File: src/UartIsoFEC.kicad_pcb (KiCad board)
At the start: 2 copper layers, 24 x 27.9 mm, 33 parts, among them J1 B3B-XH-A, P1 105444-0001, Q1 DMP3099L-13, U1 FT230XS, U2 ADUM5211

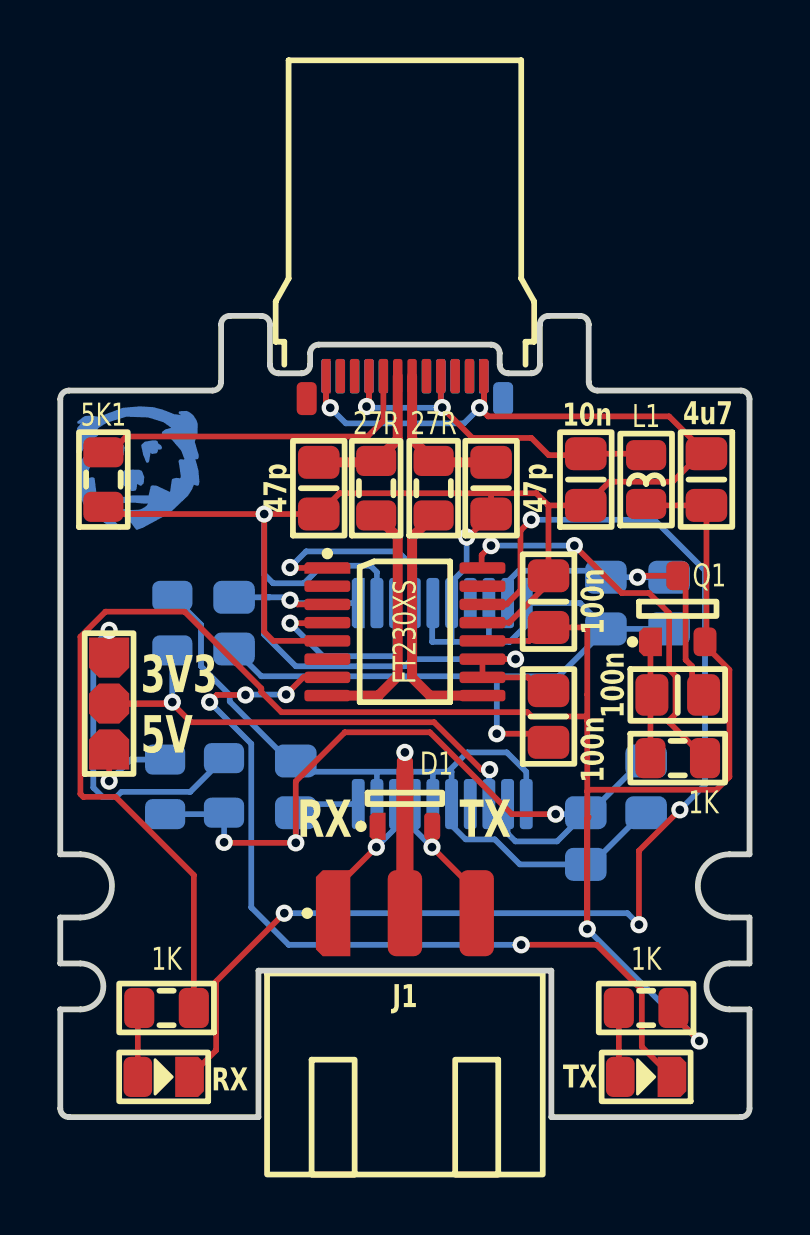
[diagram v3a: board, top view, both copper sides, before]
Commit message: Added RTS/CTS loopback
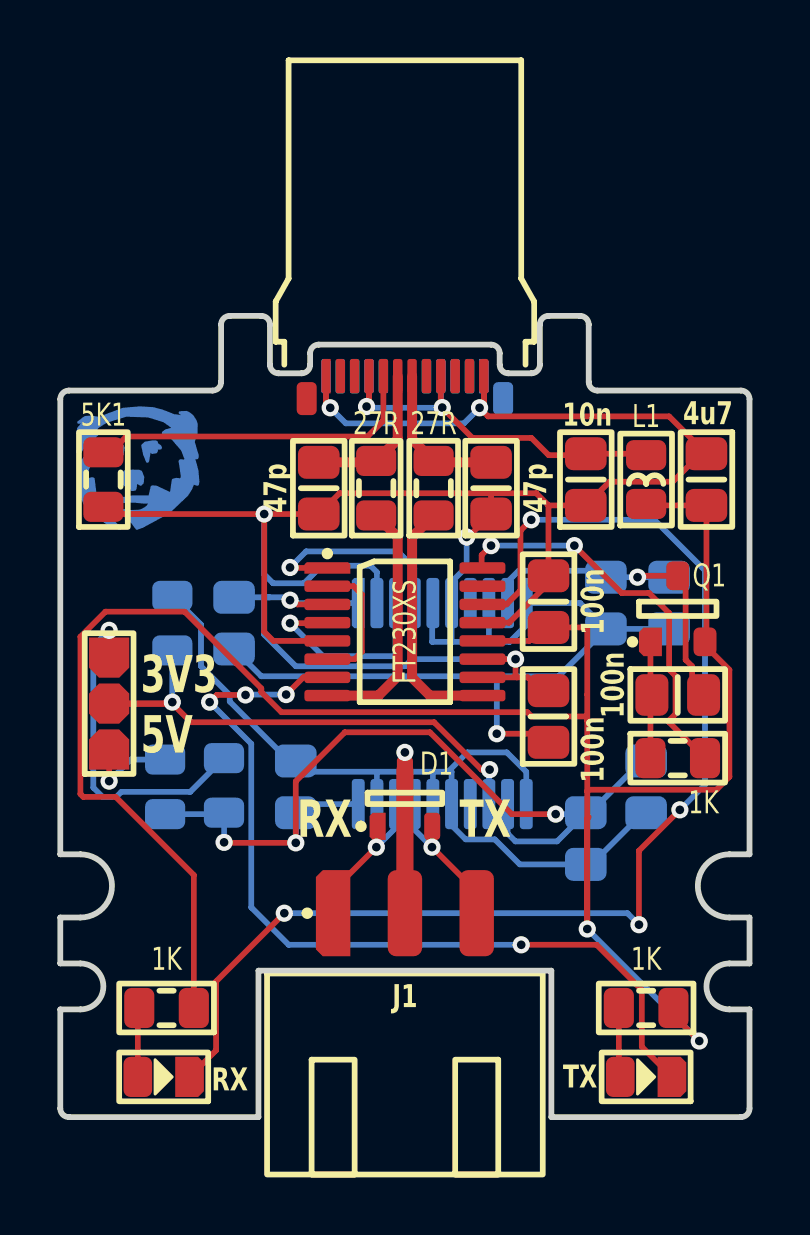
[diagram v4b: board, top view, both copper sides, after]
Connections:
- U1 pad 2: (no net) -> CTS_RTS
- U1 pad 6: (no net) -> CTS_RTS
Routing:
- net CTS_RTS: track 0.00 -> 4.62 mm
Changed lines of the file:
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@@
   (net 24 "ISO_V_SELECT_5V")
   (net 25 "ISO_V_SELECT_3V3")
+  (net 26 "CTS_RTS")
   (footprint "Medo64:R (0805)" (layer "F.Cu")
     (at 40.4 44.1 180)
@@
       (net 22 "TX") (thermal_bridge_angle 45))
     (pad "2" smd roundrect locked (at -2.7 -1.5875) (size 1.6 0.4) (layers "F.Cu" "F.Paste" "F.Mask") (roundrect_rratio 0.25)
-      (thermal_bridge_angle 45))
+      (net 26 "CTS_RTS") (thermal_bridge_angle 45))
     (pad "3" smd roundrect locked (at -2.7 -0.9525) (size 1.6 0.4) (layers "F.Cu" "F.Paste" "F.Mask") (roundrect_rratio 0.25)
       (net 12 "3V3") (thermal_bridge_angle 45))
@@
       (net 1 "GND") (thermal_bridge_angle 45))
     (pad "6" smd roundrect locked (at -2.7 0.9525) (size 1.6 0.4) (layers "F.Cu" "F.Paste" "F.Mask") (roundrect_rratio 0.25)
-      (thermal_bridge_angle 45))
+      (net 26 "CTS_RTS") (thermal_bridge_angle 45))
     (pad "7" smd roundrect locked (at -2.7 1.5875) (size 1.6 0.4) (layers "F.Cu" "F.Paste" "F.Mask") (roundrect_rratio 0.25)
       (net 17 "LED_TX") (thermal_bridge_angle 45))
@@
   (segment (start 37.899998 28) (end 37.899999 27.999999) (width 0.2) (layer "B.Cu") (net 11))
   (segment (start 28.2475 30.0475) (end 29.3 30.0475) (width 0.2) (layer "F.Cu") (net 12))
+  (segment (start 35.8525 32.54) (end 35.9 32.5875) (width 0.2) (layer "F.Cu") (net 12))
   (segment (start 34.7 31.9525) (end 35.8525 31.9525) (width 0.2) (layer "F.Cu") (net 12))
   (segment (start 28 29.8) (end 28.2475 30.0475) (width 0.2) (layer "F.Cu") (net 12))
+  (segment (start 35.9 32.5875) (end 36.2875 32.5875) (width 0.2) (layer "F.Cu") (net 12))
   (segment (start 36.2875 32.5875) (end 36.95 33.25) (width 0.2) (layer "F.Cu") (net 12))
-  (segment (start 34.7 32.5875) (end 36.2875 32.5875) (width 0.2) (layer "F.Cu") (net 12))
-  (segment (start 34.7 32.5875) (end 34.7 31.9525) (width 0.2) (layer "F.Cu") (net 12))
+  (segment (start 34.7 32.5875) (end 35.9 32.5875) (width 0.2) (layer "F.Cu") (net 12))
+  (segment (start 35.8525 31.9525) (end 35.8525 32.54) (width 0.2) (layer "F.Cu") (net 12))
   (via (at 35.8525 31.9525) (size 0.6) (drill 0.3) (layers "F.Cu" "B.Cu") (net 12))
   (via (at 28 29.9) (size 0.6) (drill 0.3) (layers "F.Cu" "B.Cu") (net 12))
@@
   (segment (start 24.525 36.575) (end 22.125 36.575) (width 0.2) (layer "B.Cu") (net 25))
   (segment (start 25.7 35.4) (end 24.525 36.575) (width 0.2) (layer "B.Cu") (net 25))
+  (segment (start 30.2125 29.4125) (end 29.3 29.4125) (width 0.2) (layer "F.Cu") (net 26))
+  (segment (start 30.5 31.7) (end 30.5 29.7) (width 0.2) (layer "F.Cu") (net 26))
+  (segment (start 30.2475 31.9525) (end 30.5 31.7) (width 0.2) (layer "F.Cu") (net 26))
+  (segment (start 30.5 29.7) (end 30.2125 29.4125) (width 0.2) (layer "F.Cu") (net 26))
+  (segment (start 29.3 31.9525) (end 30.2475 31.9525) (width 0.2) (layer "F.Cu") (net 26))
 )

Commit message: Moved LEDs to bottom
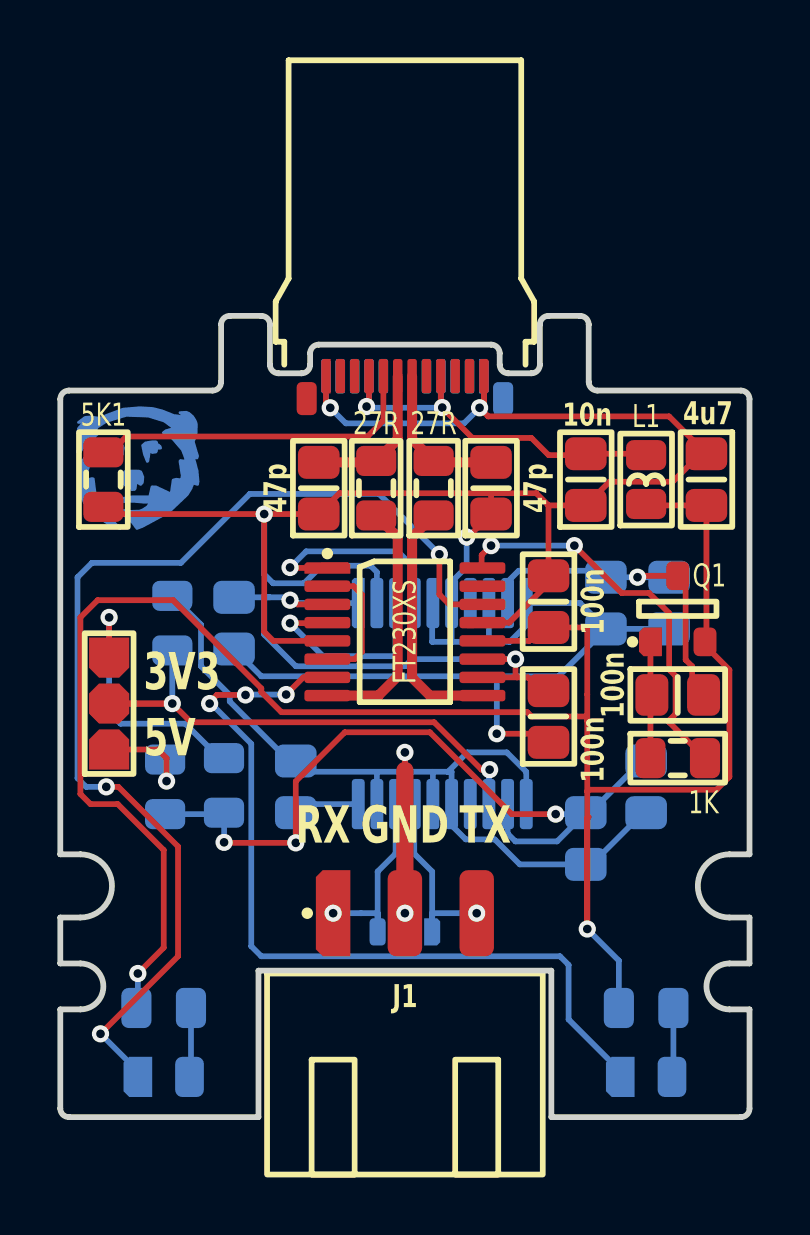
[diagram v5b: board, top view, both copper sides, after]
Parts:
- D1, DS1, DS2, R3, R4: moved to B.Cu
- moved D1 3.68 mm to (32.0, 40.5), turned to 180 degrees
- moved R3 0.10 mm to (23.6, 44.1), turned to 0 degrees
- turned DS1 to 0 degrees
- turned DS2 to 0 degrees
- turned R4 to 0 degrees
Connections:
- D1 pad 1: ISO_RX -> ISO_TX
- D1 pad 2: ISO_TX -> ISO_RX
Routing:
- net LED_RX: track 43.8 -> 38.7 mm, vias 4 -> 3
- net 5V: track 76.7 -> 73.6 mm
- net ISO_V_SELECT_3V3: track 11.9 -> 9.21 mm
- net ISO_TX: track 3.95 -> 6.17 mm
- net ISO_RX: track 3.91 -> 6.10 mm
- net ISO_GND: track 34.3 -> 35.7 mm, vias 1 -> 2
- net LED_TX: track 30.5 -> 29.3 mm, vias 4 -> 3
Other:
- board text added: "GND"

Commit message: Refactored LED control
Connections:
- R3 pad 1: 5V -> 5V_SWITCHED
- R4 pad 1: 5V -> 5V_SWITCHED
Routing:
- net 5V: track 73.6 -> 14.9 mm, vias 2 -> 0
- net 5V_SWITCHED: track 10.5 -> 49.6 mm, vias 1 -> 5
- net PWREN#: track 13.8 -> 15.1 mm

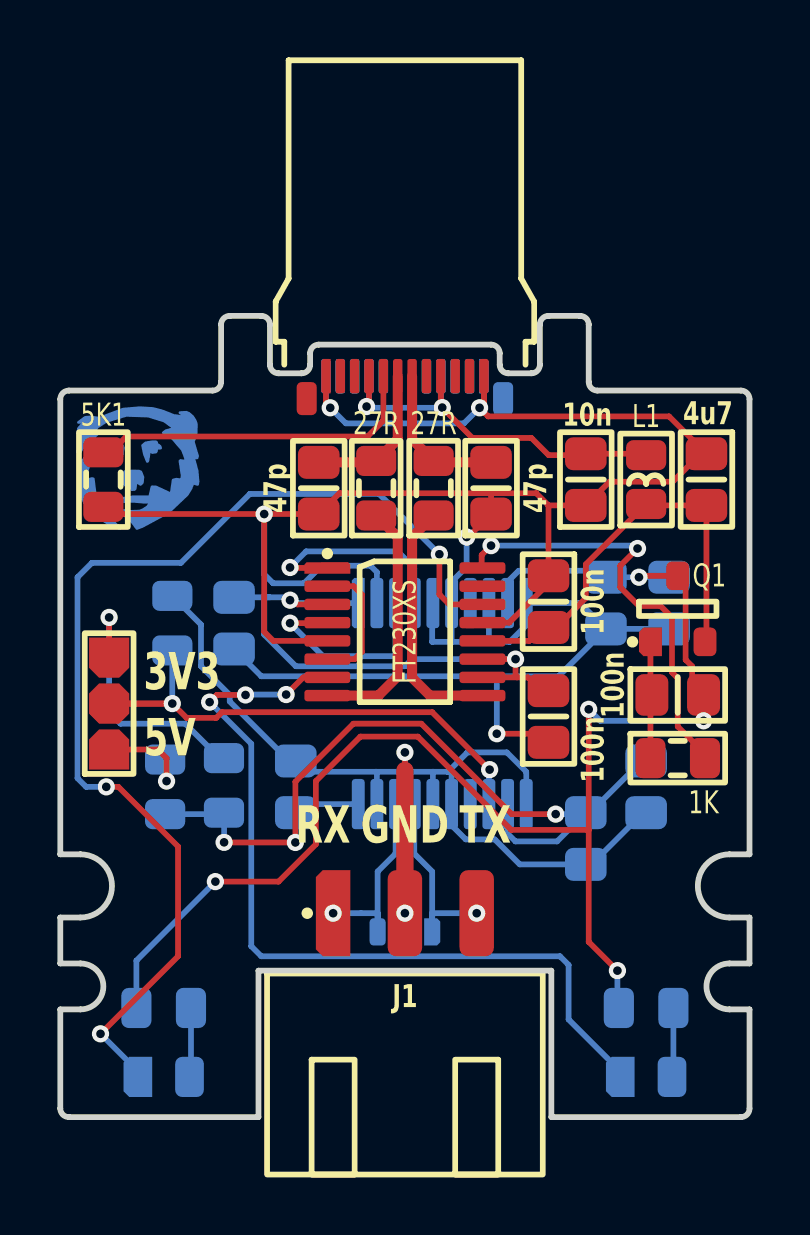
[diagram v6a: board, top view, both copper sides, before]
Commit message: Removed internal RTS/CTS connection
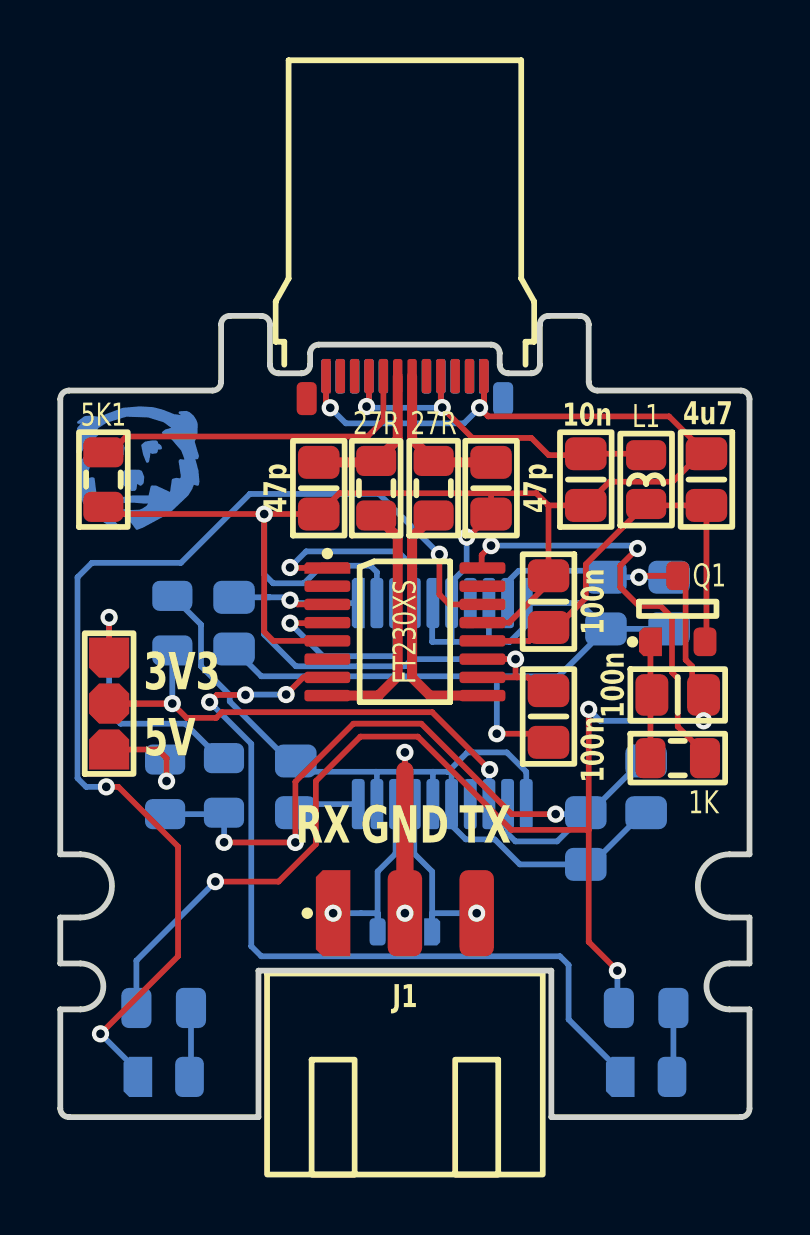
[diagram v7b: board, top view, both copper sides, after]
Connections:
- U1 pad 2: CTS_RTS -> (no net)
- U1 pad 6: CTS_RTS -> (no net)
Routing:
- net CTS_RTS: track 4.62 -> 0.00 mm
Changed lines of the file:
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@@
   (net 24 "ISO_V_SELECT_5V")
   (net 25 "ISO_V_SELECT_3V3")
-  (net 26 "CTS_RTS")
   (footprint "Medo64:C (0805)" (layer "F.Cu")
     (at 35 26 90)
@@
       (net 22 "TX") (thermal_bridge_angle 45))
     (pad "2" smd roundrect locked (at -2.7 -1.5875) (size 1.6 0.4) (layers "F.Cu" "F.Paste" "F.Mask") (roundrect_rratio 0.25)
-      (net 26 "CTS_RTS") (thermal_bridge_angle 45))
+      (thermal_bridge_angle 45))
     (pad "3" smd roundrect locked (at -2.7 -0.9525) (size 1.6 0.4) (layers "F.Cu" "F.Paste" "F.Mask") (roundrect_rratio 0.25)
       (net 12 "3V3") (thermal_bridge_angle 45))
@@
       (net 1 "GND") (thermal_bridge_angle 45))
     (pad "6" smd roundrect locked (at -2.7 0.9525) (size 1.6 0.4) (layers "F.Cu" "F.Paste" "F.Mask") (roundrect_rratio 0.25)
-      (net 26 "CTS_RTS") (thermal_bridge_angle 45))
+      (thermal_bridge_angle 45))
     (pad "7" smd roundrect locked (at -2.7 1.5875) (size 1.6 0.4) (layers "F.Cu" "F.Paste" "F.Mask") (roundrect_rratio 0.25)
       (net 17 "LED_TX") (thermal_bridge_angle 45))
@@
   (segment (start 21.7 33.8) (end 21.7 30.5) (width 0.2) (layer "B.Cu") (net 25))
   (segment (start 25.55 35.4) (end 24.35 34.2) (width 0.2) (layer "B.Cu") (net 25))
-  (segment (start 30.2125 29.4125) (end 29.3 29.4125) (width 0.2) (layer "F.Cu") (net 26))
-  (segment (start 30.5 31.7) (end 30.5 29.7) (width 0.2) (layer "F.Cu") (net 26))
-  (segment (start 30.2475 31.9525) (end 30.5 31.7) (width 0.2) (layer "F.Cu") (net 26))
-  (segment (start 30.5 29.7) (end 30.2125 29.4125) (width 0.2) (layer "F.Cu") (net 26))
-  (segment (start 29.3 31.9525) (end 30.2475 31.9525) (width 0.2) (layer "F.Cu") (net 26))
 )

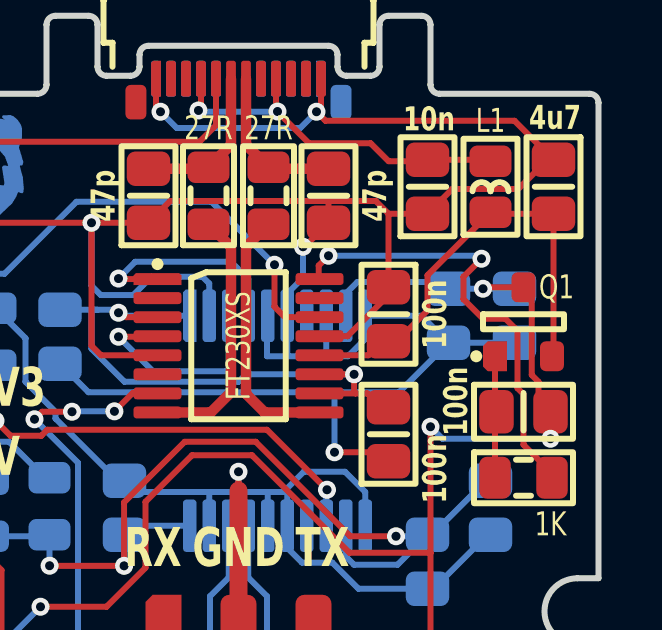
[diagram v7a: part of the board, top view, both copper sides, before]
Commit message: Added missing PWREN pullup resistor
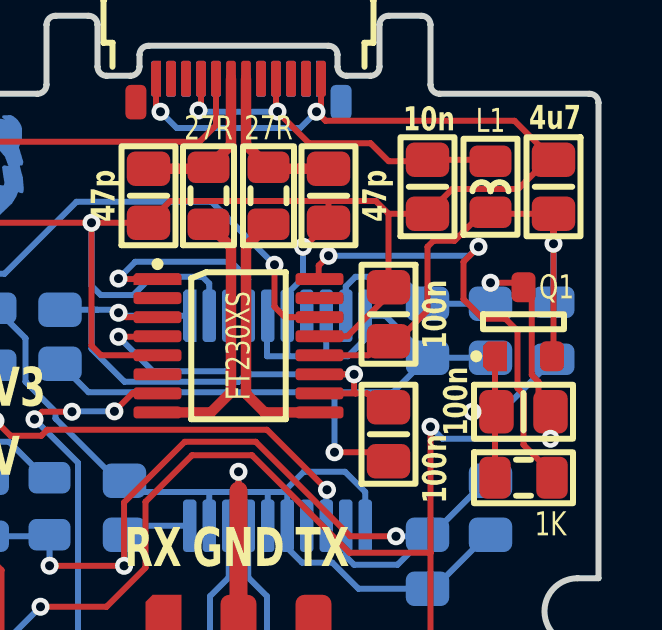
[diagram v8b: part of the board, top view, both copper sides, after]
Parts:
- added R10: 100K, Medo64:R (0805), B.Cu at (42.5, 30.5)
- moved C12 0.94 mm to (40.4, 30.5)
- moved C7 0.86 mm to (38.3, 30.5)
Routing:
- net PWREN#': track 4.00 -> 8.22 mm, vias 0 -> 1
- net 5V: track 14.9 -> 18.4 mm, vias 0 -> 1
- net 5V_SWITCHED: track 49.6 -> 50.4 mm
- net GND: track 94.9 -> 94.2 mm
